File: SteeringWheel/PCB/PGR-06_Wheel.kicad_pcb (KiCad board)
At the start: 2 copper layers, 71 parts, among them IC1 LM2575HVS-5.0_NOPB, J14 SWD, SW1 SW_SPDT, U1 MCP2561-E-SN, U2 MCP2561-E-SN, U3 LM2575HVS-3.3_NOPB, U6 STM32F405RGT6, Y1 16MHz

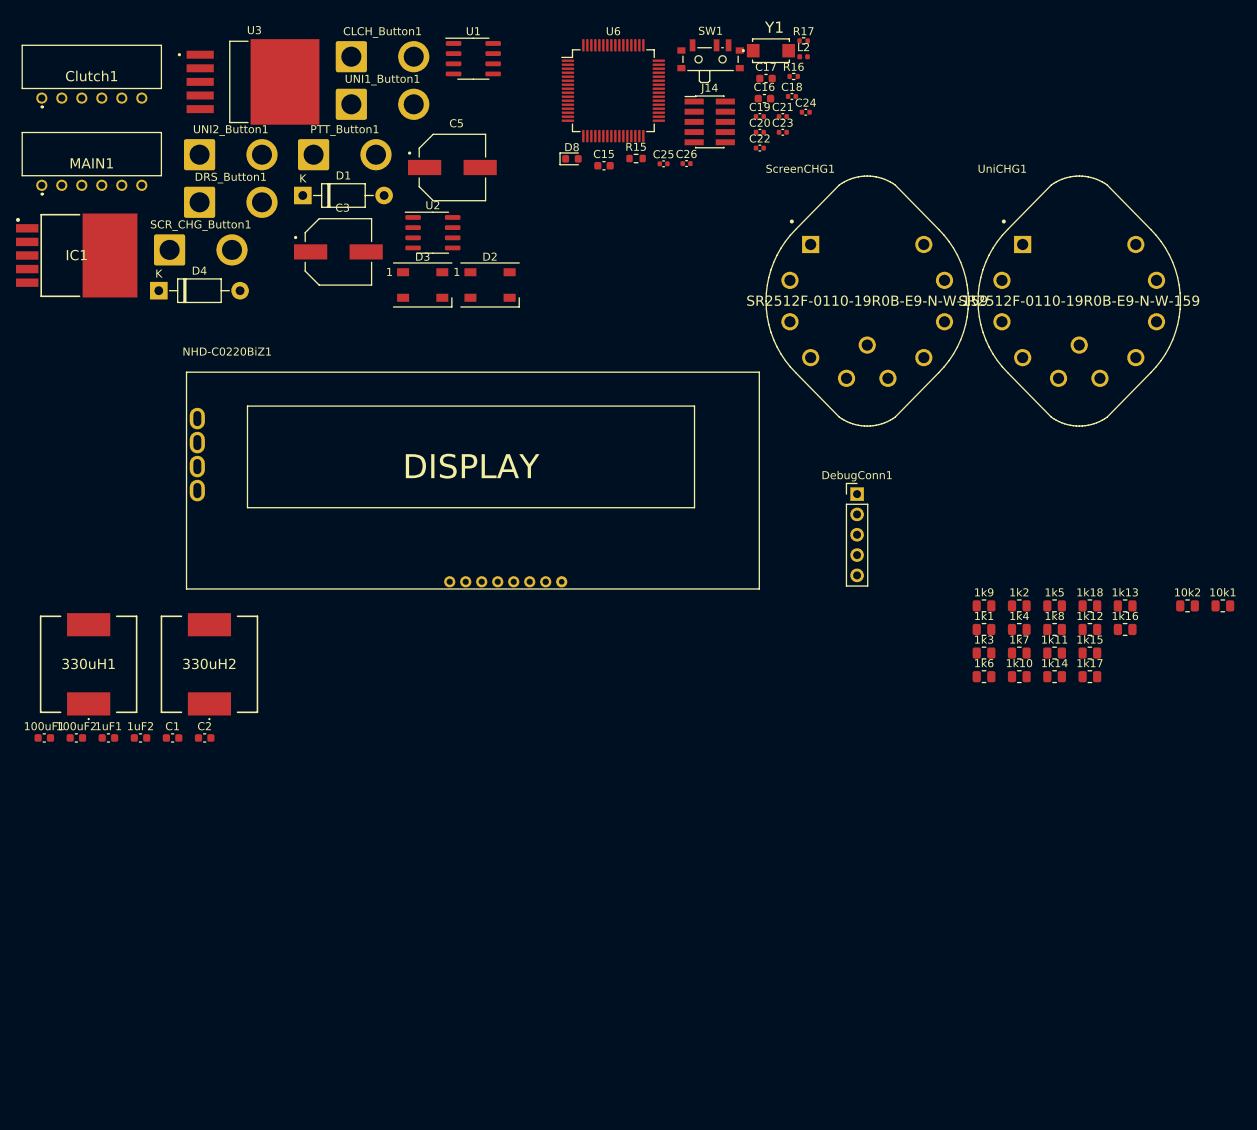
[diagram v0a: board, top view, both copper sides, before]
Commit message: New brd for steering wheel
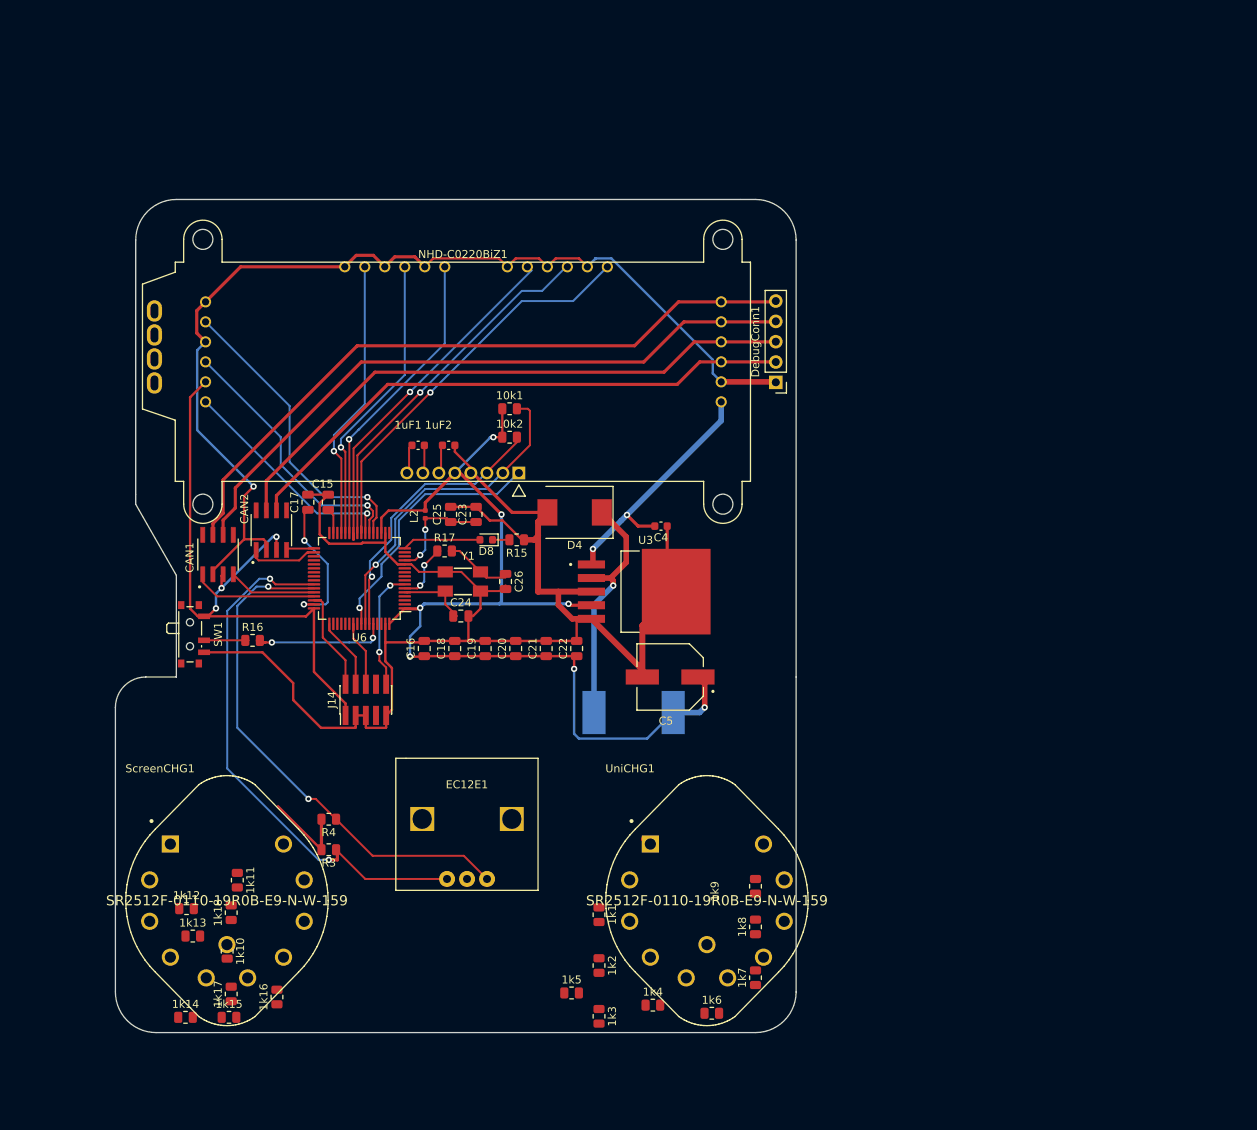
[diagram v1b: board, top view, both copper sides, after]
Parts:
- removed 100uF1, 100uF2, C1, C2: C_Small, Capacitor_SMD:C_0603_1608Metric
- removed 330uH1: L_Small, PGR-06_Additional:7447707331
- removed C3: 16SVPG330MX, 16SVPG330MX:CAP_16SVPG330MX
- removed CLCH_Button1, DRS_Button1, PTT_Button1, SCR_CHG_Button1, UNI1_Button1, UNI2_Button1: SW_Push, Connector_Wire:SolderWire-2sqmm_1x02_P7.8mm_D2mm_OD3.9mm
- removed D1: 1N5819, Diode_THT:D_DO-41_SOD81_P10.16mm_Horizontal
- removed D2, D3: WS2812B, LED_SMD:LED_WS2812B_PLCC4_5.0x5.0mm_P3.2mm
- removed IC1: LM2575HVS-5.0_NOPB, LM2575HVS-5.0_NOPB:TO170P1435X465-6N
- removed U1, U2: MCP2561-E-SN, Package_SO:SOIC-8_3.9x4.9mm_P1.27mm
- added BUTTONS_CONN1: 22-05-7065, 22-05-7065:22057065, B.Cu at (104.8, 74.3)
- added BUTTONS_CONN2: 22-05-7065, 22-05-7065:22057065, B.Cu at (125.1, 74.3)
- added C4: 100uF, Capacitor_SMD:C_0603_1608Metric, F.Cu at (138.0, 109.4)
- added CAN1: SN65HVD230MDREP, PGR-06_Additional:SOIC127P599X175-8N, F.Cu at (82.7, 113.0)
- added CAN2: SN65HVD230MDREP, PGR-06_Additional:SOIC127P599X175-8N, F.Cu at (89.3, 109.9)
- added EC12E1: EC12E1220405, PGR-06_Additional:EC12E1220405, F.Cu at (113.8, 141.2)
- added R3: 10k, Resistor_SMD:R_0805_2012Metric, F.Cu at (96.5, 149.9)
- added R4: 10k, Resistor_SMD:R_0805_2012Metric, F.Cu at (96.5, 146.1)
- C15, C16, C17: footprint Capacitor_SMD:C_0603_1608Metric -> Capacitor_SMD:C_0805_2012Metric
- C18, C19, C20, C21, C22, C23, C24, C25, C26: footprint Capacitor_SMD:C_0402_1005Metric -> Capacitor_SMD:C_0805_2012Metric
- Clutch1, MAIN1: moved to B.Cu
- D4: footprint Diode_THT:D_DO-41_SOD81_P10.16mm_Horizontal -> Diode_SMD:D_SMC
- L3.3: renamed from 330uH2; value L_Small -> 330uH; moved to B.Cu
- NHD-C0220BiZ1: footprint PGR-06_Additional:NHD-C0220BiZ-FS(RGB)-FBW-3VM -> PGR-06_Additional:NHD-C0220BiZ-FS(RGB)-FBW-3VM-NEW
- R15: footprint Resistor_SMD:R_0603_1608Metric -> Resistor_SMD:R_0805_2012Metric
- R16, R17: footprint Resistor_SMD:R_0402_1005Metric -> Resistor_SMD:R_0805_2012Metric
- Y1: footprint PGR-06_Additional:SODFL5326X110N -> PGR-06_Additional:OSCCC500X320X110-4N
- moved 1k13 123.6 mm to (79.5, 160.7)
- moved 1k12 118.2 mm to (78.7, 157.2)
- moved 1k15 116.8 mm to (84.1, 170.8)
- moved 1k14 116.7 mm to (78.6, 170.8)
- moved 1k16 115.6 mm to (90.0, 168.3), turned to 90 degrees
- moved 1k17 114.4 mm to (84.3, 167.9), turned to 90 degrees
- moved 1k18 114.0 mm to (84.3, 157.7), turned to 90 degrees
- moved ScreenCHG1 109.6 mm to (83.8, 156.2)
- moved 1k11 106.0 mm to (85.1, 153.7), turned to 270 degrees
- moved 1k10 104.8 mm to (83.8, 162.6), turned to 270 degrees
- moved R16 97.7 mm to (87.0, 123.7)
- moved SW1 97.0 mm to (79.5, 122.9), turned to 270 degrees
- moved 10k1 92.5 mm to (119.1, 94.7)
- moved UniCHG1 88.2 mm to (143.8, 156.2)
- moved 10k2 87.3 mm to (119.1, 98.3)
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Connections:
- Clutch1 pad 1: CS_P6 -> /STM32F405RGT6/CLCH_CS
- Clutch1 pad 3: DO_P4 -> /STM32F405RGT6/CLCH_DO
- Clutch1 pad 5: CLK -> /STM32F405RGT6/CLCH_CLK
- DebugConn1 pad 1: CAN2_H -> GND
- DebugConn1 pad 3: CAN1_H -> CAN2_H
- DebugConn1 pad 5: GND -> CAN1_H
- J14 pad 7: Net-(J14-Pad7) -> (no net)
- J14 pad 8: Net-(J14-Pad8) -> (no net)
- MAIN1 pad 1: CAN1_L -> CAN1_H
- MAIN1 pad 2: CAN1_H -> CAN1_L
- MAIN1 pad 3: CAN2_L -> CAN2_H
- MAIN1 pad 4: CAN2_H -> CAN2_L
- NHD-C0220BiZ1 pad 10: Net-(NHD-C0220BiZ1-Pad10) -> (no net)
- NHD-C0220BiZ1 pad 11: Net-(NHD-C0220BiZ1-Pad11) -> (no net)
- NHD-C0220BiZ1 pad 12: Net-(NHD-C0220BiZ1-Pad12) -> (no net)
- NHD-C0220BiZ1 pad 9: Net-(NHD-C0220BiZ1-Pad9) -> +3V3
- U6 pad 10: Net-(U6-Pad10) -> (no net)
- U6 pad 11: Net-(U6-Pad11) -> (no net)
- U6 pad 14: /STM32F405RGT6/ROT_UNI -> (no net)
- U6 pad 17: Net-(U6-Pad17) -> (no net)
- U6 pad 2: Net-(U6-Pad2) -> (no net)
- U6 pad 20: Net-(U6-Pad20) -> (no net)
- U6 pad 21: Net-(U6-Pad21) -> /STM32F405RGT6/CLCH_CLK
- U6 pad 22: Net-(U6-Pad22) -> /STM32F405RGT6/CLCH_DO
- U6 pad 23: Net-(U6-Pad23) -> /STM32F405RGT6/CLCH_CS
- U6 pad 29: Net-(U6-Pad29) -> /STM32F405RGT6/BTN_UNI2
- U6 pad 3: Net-(U6-Pad3) -> (no net)
- U6 pad 30: Net-(U6-Pad30) -> (no net)
- U6 pad 35: Net-(U6-Pad35) -> (no net)
- U6 pad 36: Net-(U6-Pad36) -> (no net)
- U6 pad 37: /STM32F405RGT6/BTN_UNI2 -> (no net)
- U6 pad 38: Net-(U6-Pad38) -> (no net)
- U6 pad 39: /STM32F405RGT6/LED_DATA -> (no net)
- U6 pad 4: Net-(U6-Pad4) -> (no net)
- U6 pad 40: Net-(U6-Pad40) -> (no net)
- U6 pad 41: Net-(U6-Pad41) -> (no net)
- U6 pad 42: Net-(U6-Pad42) -> /Rotaries/ENC_A
- U6 pad 43: Net-(U6-Pad43) -> /Rotaries/ENC_B
- U6 pad 50: Net-(U6-Pad50) -> (no net)
- U6 pad 51: Net-(U6-Pad51) -> (no net)
- U6 pad 52: Net-(U6-Pad52) -> (no net)
- U6 pad 53: Net-(U6-Pad53) -> (no net)
- U6 pad 54: Net-(U6-Pad54) -> (no net)
- U6 pad 56: Net-(U6-Pad56) -> (no net)
- U6 pad 61: Net-(U6-Pad61) -> (no net)
- U6 pad 62: Net-(U6-Pad62) -> (no net)
- U6 pad 8: Net-(U6-Pad8) -> (no net)
- U6 pad 9: Net-(U6-Pad9) -> (no net)
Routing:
- net GND: track 0.00 -> 328.4 mm, vias 0 -> 1
- net +3V3: track 0.00 -> 221.6 mm, vias 0 -> 10
- net CAN1_H: track 0.00 -> 85.7 mm
- net CAN1_L: track 0.00 -> 82.7 mm
- net CAN2_H: track 0.00 -> 74.6 mm
- net CAN2_L: track 0.00 -> 71.2 mm
- net /Rotaries/ENC_A: track 0.00 -> 68.2 mm, vias 0 -> 2
- net /Rotaries/ENC_B: track 0.00 -> 65.0 mm, vias 0 -> 2
- net /STM32F405RGT6/BTN_SCR: track 0.00 -> 50.6 mm, vias 0 -> 1
- net /STM32F405RGT6/BTN_PTT: track 0.00 -> 45.7 mm, vias 0 -> 1
- net /STM32F405RGT6/BTN_CLCH: track 0.00 -> 44.5 mm, vias 0 -> 1
- net /STM32F405RGT6/I2C_SCL: track 0.00 -> 41.3 mm, vias 0 -> 1
- net /STM32F405RGT6/CLCH_CLK: track 0.00 -> 38.6 mm, vias 0 -> 1
- net /STM32F405RGT6/BTN_UNI1: track 0.00 -> 38.4 mm, vias 0 -> 1
- net /STM32F405RGT6/BTN_DRS: track 0.00 -> 36.8 mm, vias 0 -> 1
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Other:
- board outline added: 85.1 x 104.1 mm
- net class 1ABuck added: clearance 0.4, trace_width 0.75, via_dia 0.8, via_drill 0.4
- net class CL2 added: clearance 0.2, trace_width 0.3, via_dia 0.8, via_drill 0.4

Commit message: Steering Wheel Update
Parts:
- removed C4: 100uF, Capacitor_SMD:C_0603_1608Metric
- removed C5: 16SVPG330MX, 16SVPG330MX:CAP_16SVPG330MX
- removed D4: 1N5819, Diode_SMD:D_SMC
- removed L3.3: 330uH, PGR-06_Additional:7447707331
- removed U3: LM2575HVS-3.3_NOPB, LM2575HVS-3.3_NOPB:VREG_TPS79625KTTR
- added C1: BD_CAP2, Capacitor_SMD:C_0805_2012Metric, F.Cu at (147.2, 126.8)
- added C2: BD_CAP1, Capacitor_SMD:C_0805_2012Metric, F.Cu at (135.8, 127.8)
- added DI1: 0Ohm, Resistor_SMD:R_0805_2012Metric, F.Cu at (143.5, 121.6)
- added G***: LOGO, PGR-06_Additional:logo, B.Cu at (142.2, 83.8)
- added G***: LOGO, PGR-06_Additional:logo, F.Cu at (124.5, 134.6)
- added H1: MountingHole, MountingHole:MountingHole_3.2mm_M3, F.Cu at (89.4, 72.6)
- added H2: MountingHole, MountingHole:MountingHole_3.2mm_M3, F.Cu at (139.2, 72.6)
- added H3: MountingHole, MountingHole:MountingHole_3.2mm_M3, F.Cu at (151.4, 135.6)
- added H4: MountingHole_Pad, MountingHole:MountingHole_3.2mm_M3_Pad_TopBottom, F.Cu at (74.2, 135.6)
- added IC_33v1: BD733L5FP-CE2, PGR-06_Additional:BD750L5FPCE2, F.Cu at (140.8, 133.9)
- added LED_B1: R_Small, Resistor_SMD:R_0805_2012Metric, B.Cu at (77.7, 83.3)
- added LED_G1: R_Small, Resistor_SMD:R_0805_2012Metric, B.Cu at (78.7, 99.1)
- added LED_R1: R_Small, Resistor_SMD:R_0805_2012Metric, B.Cu at (77.2, 102.6)
- added R_Terminator_1: 120Ohm, Resistor_SMD:R_0805_2012Metric, F.Cu at (79.2, 127.5)
- added R_Terminator_2: 120Ohm, Resistor_SMD:R_0805_2012Metric, F.Cu at (76.2, 115.3)
- added U1: LM1117-5.0, Package_TO_SOT_SMD:TO-252-2, F.Cu at (134.7, 115.3)
- 10k1, 10k2, 1k1, 1k10, 1k11, 1k12, 1k13, 1k14, 1k15, 1k16, 1k17, 1k18, 1k2, 1k3, 1k4, 1k5, 1k6, 1k7, 1k8, 1k9, 1uF1, 1uF2, R3, R4: moved to B.Cu
- CAN1, CAN2: value SN65HVD230MDREP -> MCP2561-E-P; footprint PGR-06_Additional:SOIC127P599X175-8N -> Package_DIP:DIP-8_W7.62mm
- moved SW1 56.5 mm to (115.6, 166.4), turned to 0 degrees
- moved MAIN1 51.9 mm to (117.3, 132.8), turned to 180 degrees
- moved DebugConn1 48.6 mm to (132.1, 135.6)
- moved R16 47.2 mm to (115.6, 161.3), turned to 90 degrees
- moved CAN1 19.6 mm to (89.4, 131.4), turned to 180 degrees
- moved 1k5 17.0 mm to (143.8, 167.9)
- moved 1k17 13.5 mm to (91.2, 156.2)
- moved 1k10 12.5 mm to (76.7, 152.3)
- moved 1k3 12.1 mm to (136.5, 160.3)
- moved 1k2 10.1 mm to (136.5, 156.3)
- moved CAN2 9.78 mm to (86.9, 119.4), turned to 180 degrees
- moved R4 9.66 mm to (102.3, 153.8)
- moved 1k11 8.91 mm to (76.6, 156.3)
- moved 1k18 8.85 mm to (91.2, 152.1)
- moved 1k1 8.36 mm to (136.5, 152.4)
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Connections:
- CAN1 pad 3: +3V3 -> +5V
- CAN1 pad 8: (no net) -> GND
- CAN2 pad 3: +3V3 -> +5V
- CAN2 pad 8: (no net) -> GND
- MAIN1 pad 1: CAN1_H -> CAN2_L
- MAIN1 pad 2: CAN1_L -> CAN2_H
- MAIN1 pad 3: CAN2_H -> CAN1_L
- MAIN1 pad 4: CAN2_L -> CAN1_H
- MAIN1 pad 6: +12V -> VDD
- NHD-C0220BiZ1 pad 10: (no net) -> Net-(LED_R1-Pad2)
- NHD-C0220BiZ1 pad 11: (no net) -> Net-(LED_G1-Pad2)
- NHD-C0220BiZ1 pad 12: (no net) -> Net-(LED_B1-Pad2)
- U6 pad 15: /Rotaries/ROT_SCR -> (no net)
- U6 pad 35: (no net) -> /STM32F405RGT6/LED_B
- U6 pad 36: (no net) -> /STM32F405RGT6/LED_G
- U6 pad 37: (no net) -> /STM32F405RGT6/LED_R
- U6 pad 40: (no net) -> /Rotaries/ROT_UNI
- U6 pad 41: (no net) -> /Rotaries/ROT_SCR
- UniCHG1 pad 11: /Rotaries/ROT_SCR -> /Rotaries/ROT_UNI
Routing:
- net /Rotaries/ROT_UNI: track 0.00 -> 91.4 mm, vias 0 -> 1
- net GND: track 328.4 -> 416.3 mm, vias 1 -> 14
- net +5V: track 0.00 -> 87.0 mm, vias 0 -> 1
- net VDD: track 0.00 -> 69.8 mm
- net /Rotaries/ROT_SCR: track 0.00 -> 50.2 mm, vias 0 -> 2
- net /STM32F405RGT6/LED_B: track 0.00 -> 37.2 mm, vias 0 -> 1
- net BOOT0: track 18.2 -> 51.5 mm, vias 2 -> 4
- net +12V: track 31.1 -> 0.00 mm, vias 2 -> 0
- net Net-(D4-Pad1): track 30.6 -> 0.00 mm, vias 1 -> 0
- net CAN1_H: track 85.7 -> 60.0 mm
- net /STM32F405RGT6/LED_G: track 0.00 -> 24.3 mm, vias 0 -> 3
- net /STM32F405RGT6/LED_R: track 0.00 -> 21.5 mm, vias 0 -> 3
- net CAN1_L: track 82.7 -> 61.8 mm
- net /Rotaries/ENC_A: track 68.2 -> 48.5 mm, vias 2 -> 1
- net Net-(LED_R1-Pad2): track 0.00 -> 15.5 mm
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- added copper zone on B.Cu, net +3V3
- added copper zone on F.Cu, net GND
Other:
- outline, holes or cut-outs redrawn
